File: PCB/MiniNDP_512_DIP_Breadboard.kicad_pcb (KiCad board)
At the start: 2 copper layers, 9 parts, among them J1 Conn_02x20_Odd_Even, U1 HC161, U2 HC161, U3 HC161, U4 HC138, U5 HC374, U6 AS6C4008, U7 HC32, U8 HC374

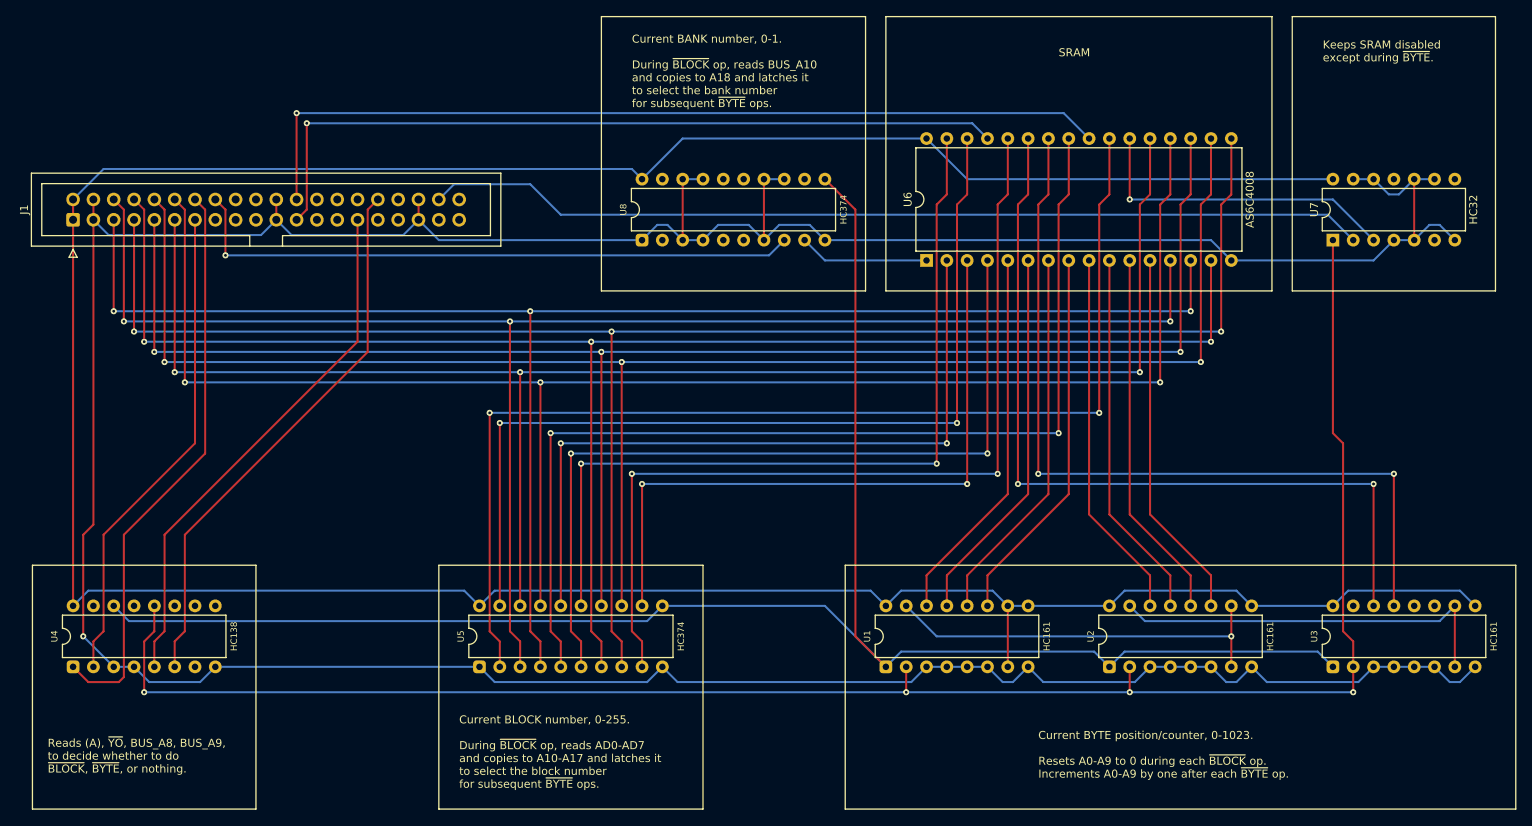
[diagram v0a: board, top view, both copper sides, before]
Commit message: notes in historical, big cap in 1M_C
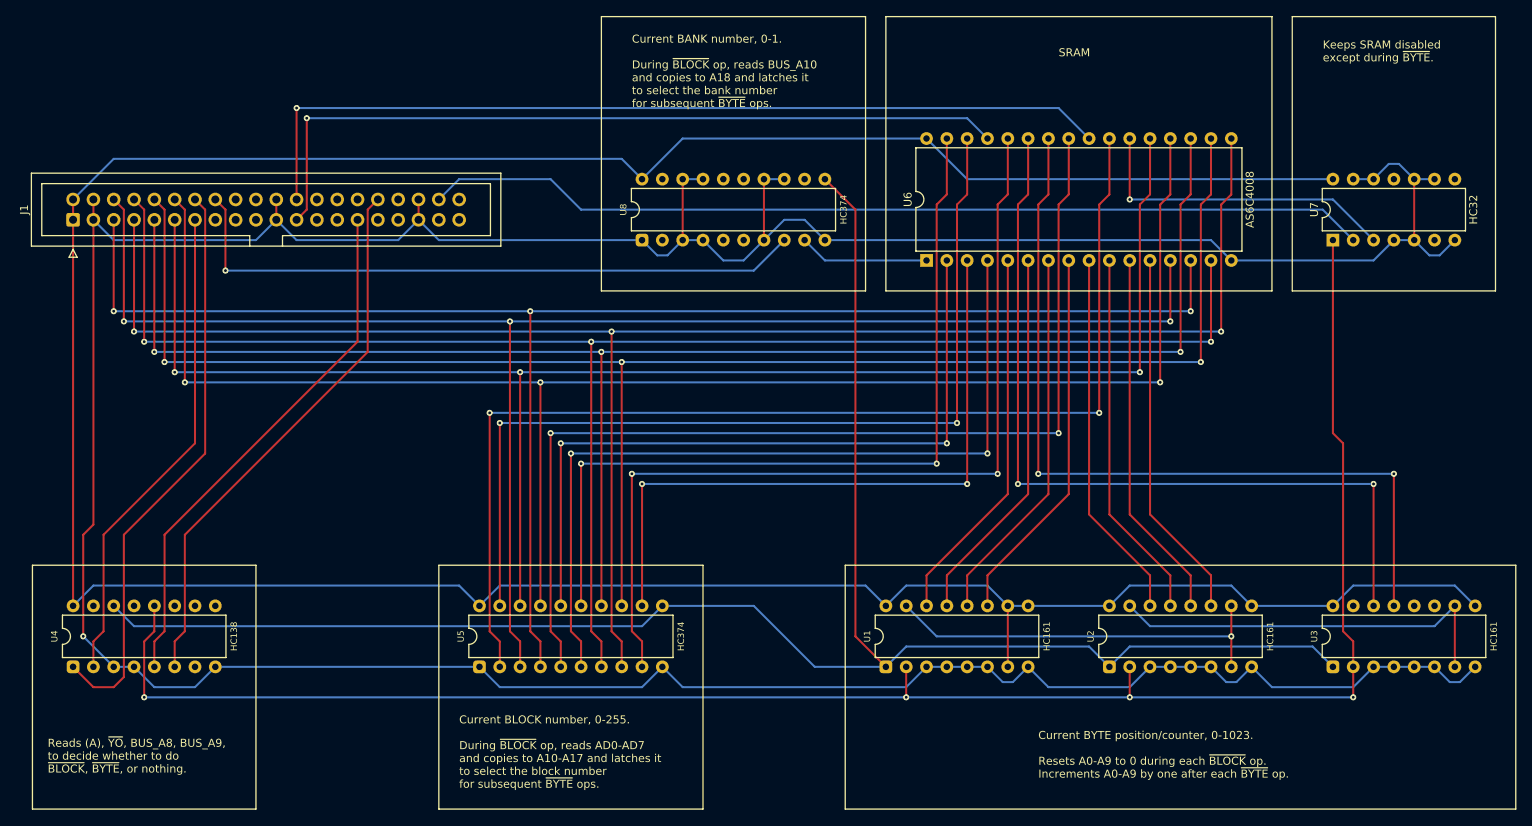
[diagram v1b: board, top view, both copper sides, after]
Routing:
- net GND: track 470.9 -> 475.6 mm
- net VBUS: track 405.4 -> 409.0 mm
- net /BUS_A10: track 78.2 -> 80.8 mm
- net /~{BYTE}: track 226.4 -> 228.9 mm
- net /~{BLOCK}: track 224.4 -> 226.0 mm
- net /~{WR}: track 98.5 -> 99.4 mm
- net /~{RD}: track 111.2 -> 112.1 mm
- net /TC1: track 49.8 -> 50.4 mm
- net /RAMRST: track 118.0 -> 118.5 mm
- net /BUS_A8: track 71.8 -> 72.4 mm
